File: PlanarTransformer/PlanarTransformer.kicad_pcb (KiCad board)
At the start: 4 copper layers, 27.8 x 21.9 mm, 5 parts

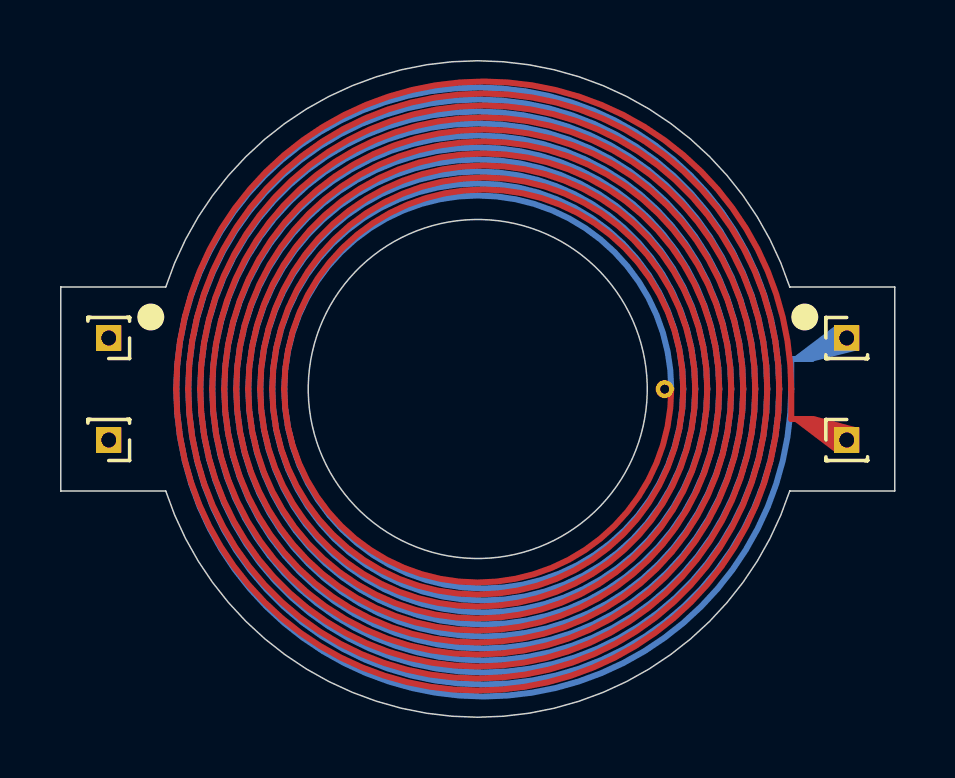
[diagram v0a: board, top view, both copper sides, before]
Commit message: rev 2 of 400V converter
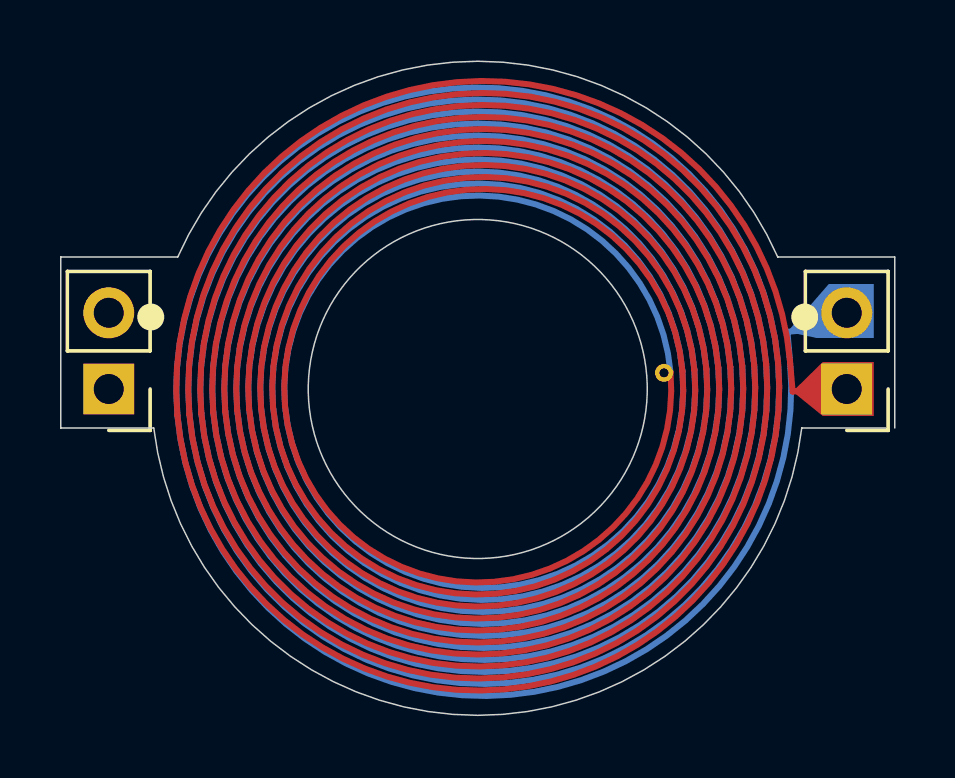
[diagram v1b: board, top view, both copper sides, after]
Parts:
- removed the REF** at (176.6, 70.7)
- removed the REF** at (176.6, 74.1)
- removed the REF** at (152.0, 74.1)
- removed the REF** at (152.0, 70.7)
- added REF**: PinHeader_1x02_P2.54mm_Vertical, Connector_PinHeader_2.54mm:PinHeader_1x02_P2.54mm_Vertical, F.Cu at (152.0, 72.4)
- added REF**: PinHeader_1x02_P2.54mm_Vertical, Connector_PinHeader_2.54mm:PinHeader_1x02_P2.54mm_Vertical, F.Cu at (176.6, 72.4)
- turned REF** to 5 degrees
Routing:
- net (no net): track 21.5 -> 26.0 mm
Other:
- board size 27.8 x 21.9 mm -> 27.8 x 21.8 mm
